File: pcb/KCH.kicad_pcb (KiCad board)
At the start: 2 copper layers, 65 x 56 mm, 153 parts, among them J1 CTBP9550/2, J2 Write EEPROM, J3 40HAT, J4 Serial, Q1 AO3407A, Q10 2N7002KDW, Q11 2N7002KDW, Q12 2N7002KDW, Q13 2N7002KDW, Q14 2N7002KDW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

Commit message: Correct reg IC to AP62300T
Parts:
- U2: value AP63200T -> AP62300T
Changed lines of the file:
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@@
 			)
 		)
-		(property "Value" "AP63200T"
+		(property "Value" "AP62300T"
 			(at 0 2.4 0)
 			(layer "F.Fab")
@@
 			)
 		)
-		(property "JLC" ""
+		(property "JLC" "C1883519"
 			(at 0 0 0)
 			(unlocked yes)

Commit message: Update blue LEDs to stocked part
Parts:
- R32, R37: value 1k -> 2k2
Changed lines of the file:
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@@
 			)
 		)
-		(property "Datasheet" "https://datasheet.lcsc.com/lcsc/1811101510_Everlight-Elec-19-217-BHC-ZL1M2RY-3T_C72041.pdf"
+		(property "Datasheet" "https://wmsc.lcsc.com/wmsc/upload/file/pdf/v2/lcsc/1810220913_Hubei-KENTO-Elec-KT-0603B_C2288.pdf"
 			(at 0 0 90)
 			(layer "F.Fab")
@@
 			)
 		)
-		(property "JLC" "C72041"
+		(property "JLC" "C2288"
 			(at 0 0 90)
 			(unlocked yes)
@@
 			)
 		)
-		(property "Value" "1k"
+		(property "Value" "2k2"
 			(at 0 1.17 90)
 			(layer "F.Fab")
@@
 			)
 		)
-		(property "JLC" "C11702"
+		(property "JLC" "C25879"
 			(at 0 0 -90)
 			(unlocked yes)
@@
 			)
 		)
-		(property "Datasheet" "https://datasheet.lcsc.com/lcsc/1811101510_Everlight-Elec-19-217-BHC-ZL1M2RY-3T_C72041.pdf"
+		(property "Datasheet" "https://wmsc.lcsc.com/wmsc/upload/file/pdf/v2/lcsc/1810220913_Hubei-KENTO-Elec-KT-0603B_C2288.pdf"
 			(at 0 0 90)
 			(layer "F.Fab")
@@
 			)
 		)
-		(property "JLC" "C72041"
+		(property "JLC" "C2288"
 			(at 0 0 90)
 			(unlocked yes)
@@
 			)
 		)
-		(property "Value" "1k"
+		(property "Value" "2k2"
 			(at 0 1.17 90)
 			(layer "F.Fab")
@@
 			)
 		)
-		(property "JLC" "C11702"
+		(property "JLC" "C25879"
 			(at 0 0 90)
 			(unlocked yes)

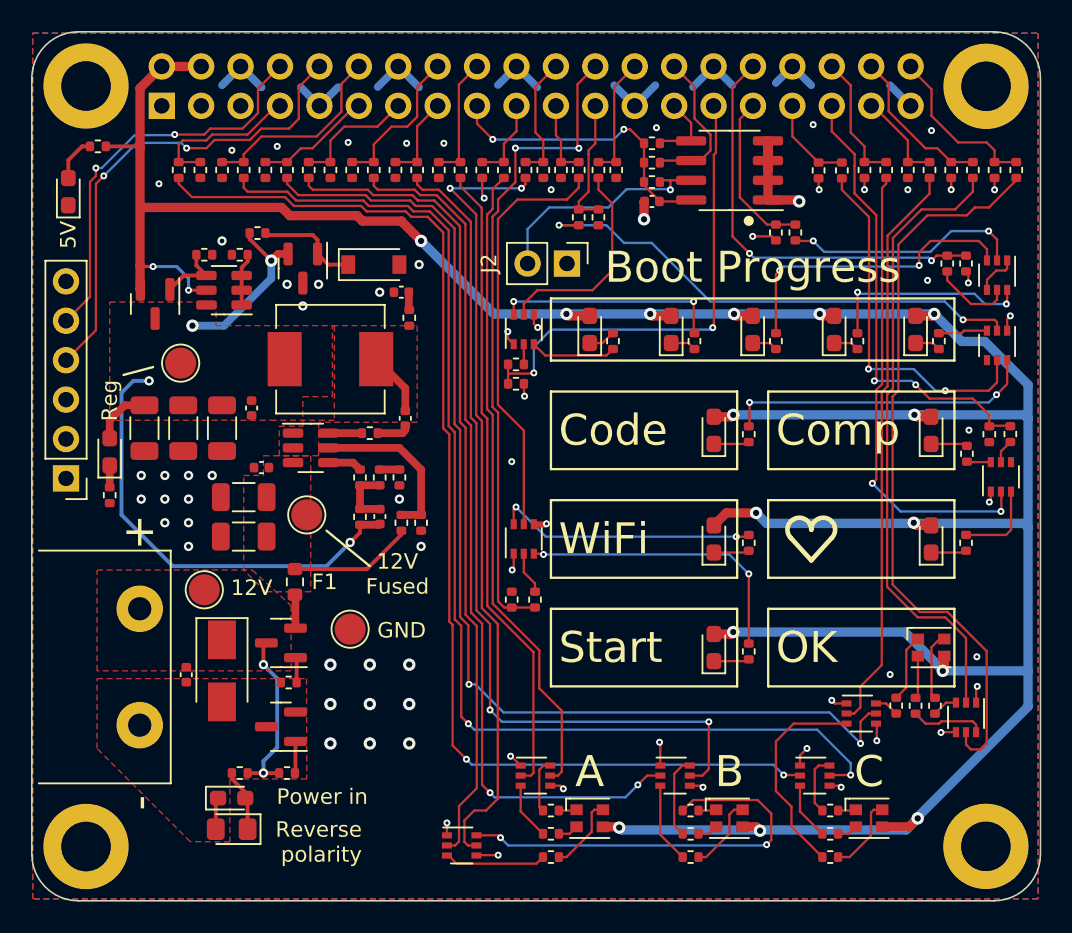
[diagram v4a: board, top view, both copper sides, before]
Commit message: Fix ERC/DRC errors from Kicad 8
Mostly outdated library symbols and aligning the schmatic to the new grid
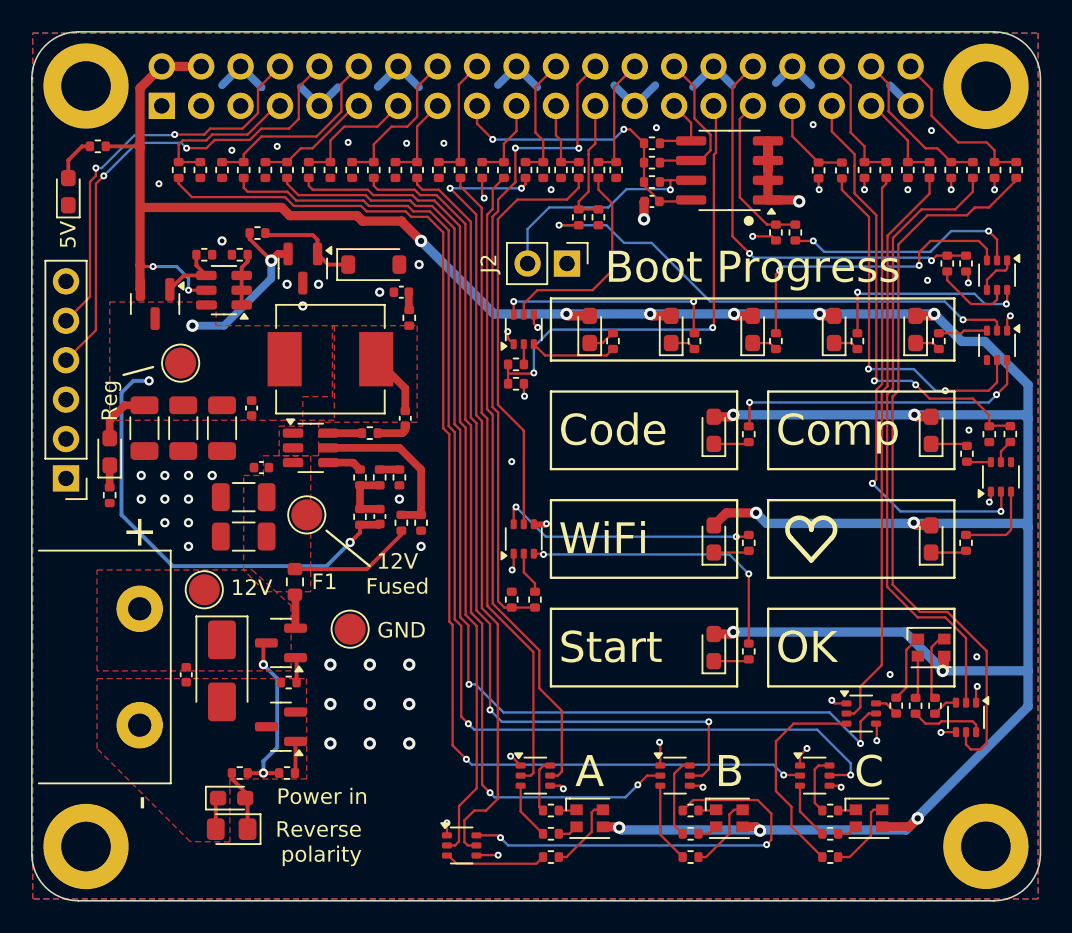
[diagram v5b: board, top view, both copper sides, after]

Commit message: Update to revision C
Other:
- board text added: "Student Robotics KCH V1 Rev C"
- board text removed: "Student Robotics KCH V1 Rev B"
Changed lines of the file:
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@@
 	(title_block
 		(title "KCH - Raspberry Pi HAT")
-		(date "2022-07-15")
-		(rev "B (S3L2)")
+		(date "2024-07-05")
+		(rev "C (S4L3)")
 		(company "Student Robotics")
 	)
@@
 		(layer "F.Fab")
 	)
-	(gr_text "Student Robotics\nKCH V1 Rev B"
+	(gr_text "Student Robotics\nKCH V1 Rev C"
 		(at 111.25 98.75 0)
 		(layer "B.SilkS")
